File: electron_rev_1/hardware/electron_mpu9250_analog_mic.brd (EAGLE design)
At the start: 22.5 x 52.7 mm, 35 parts, among them IC4 MIC_I2S_SPH0645, U1 MPU-9250, U3 OPA322AIDBVT, U4 microSD

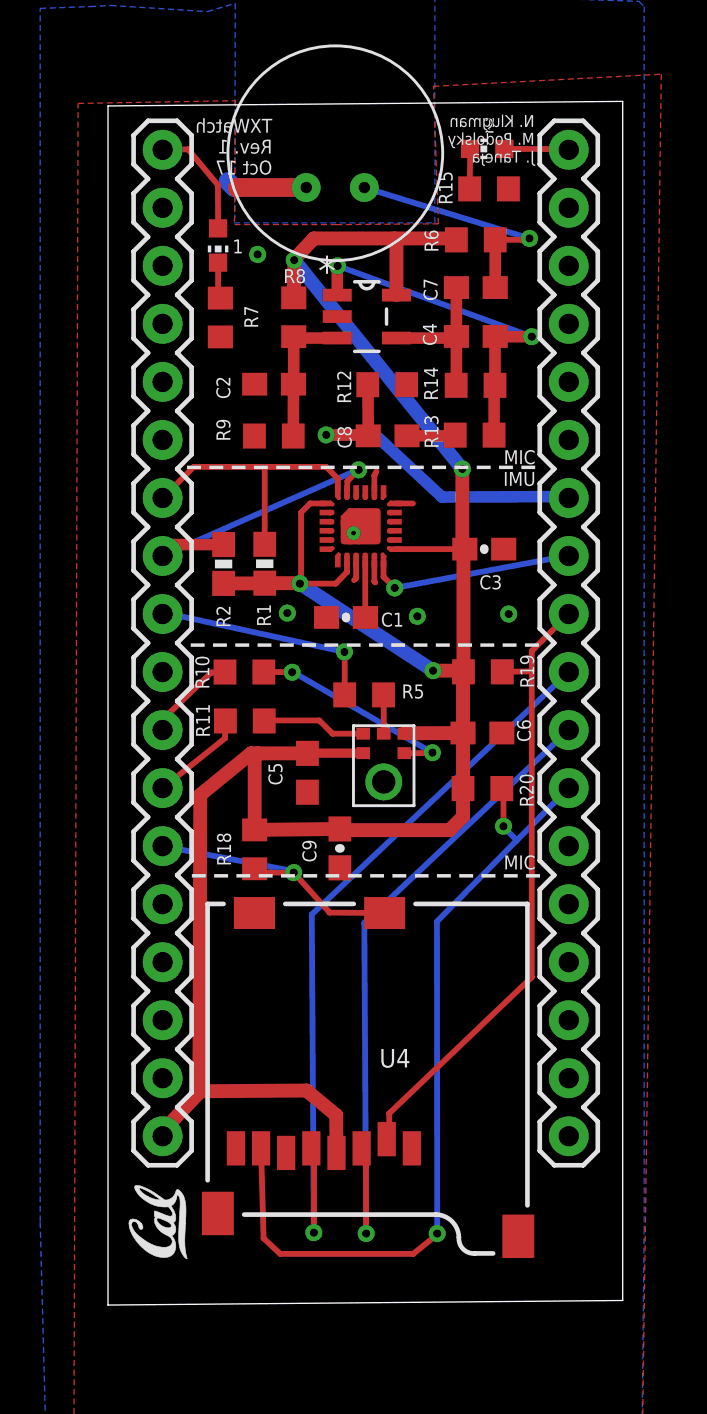
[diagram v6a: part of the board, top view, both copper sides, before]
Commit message: reroute w out gas sensor. almost ready to ship
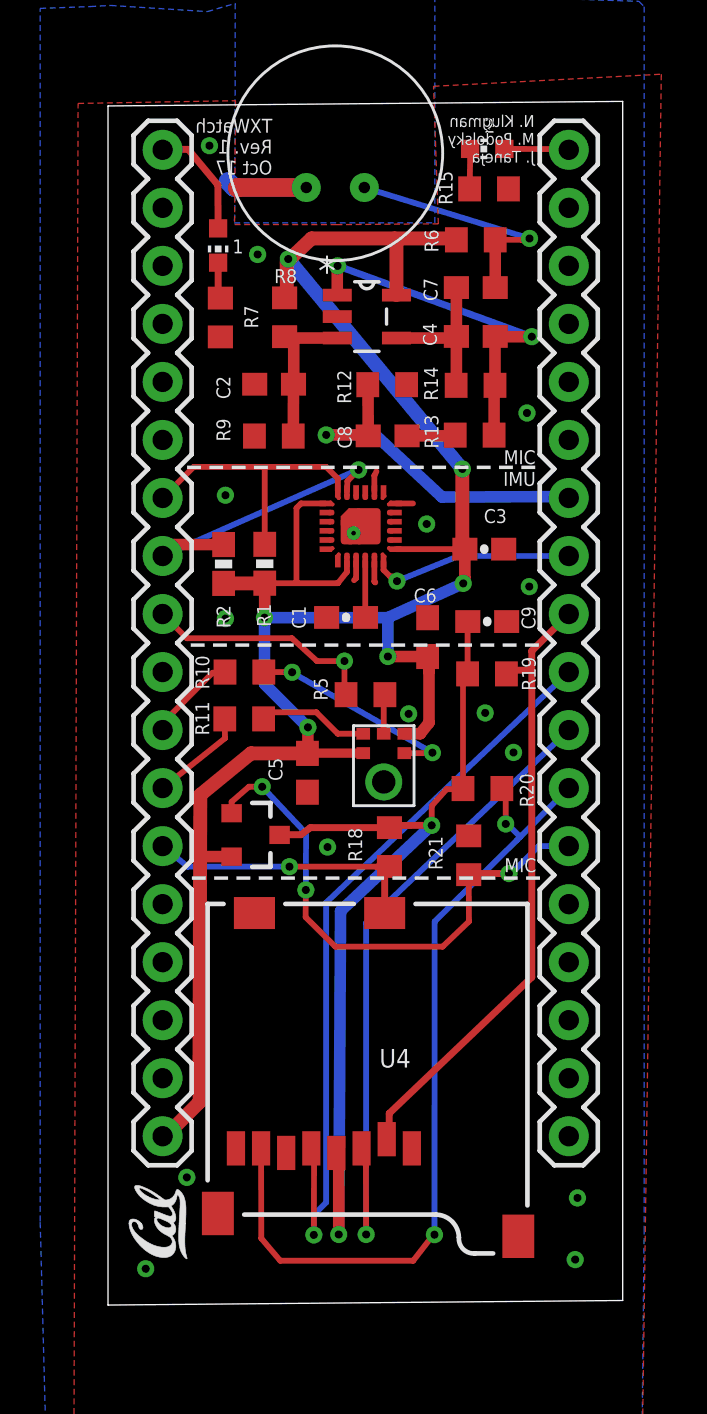
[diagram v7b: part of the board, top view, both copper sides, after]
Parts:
- added Q2: NX3008PBK, fets:SOT23-3
- added R21: 10K, resistor:R0603
- moved C9 11.8 mm to (15.8, 24.0), turned to 0 degrees
- moved R18 5.90 mm to (11.5, 14.2)
- moved C6 4.84 mm to (13.1, 23.4), turned to 90 degrees
- moved R8 0.40 mm to (6.88, 37.4)
- moved R19 0.20 mm to (15.7, 21.7)
- moved R11 0.09 mm to (5.11, 19.8)
- moved R5 0.06 mm to (10.4, 20.8)
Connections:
- new net N$10: C9.1, Q2.3, R18.2, R19.2, R20.2, U4.4
- net EN: now also Q2.1, R21.2
- net GND: now also R21.1
- net VCC: now also Q2.2; no longer C9.1, R18.2, R19.2, R20.2, U4.4
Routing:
- net N$10: track 0.00 -> 41.3 mm, vias 0 -> 2
- net EN: track 0.00 -> 23.9 mm, vias 0 -> 3
- net VCC: track 108.8 -> 93.7 mm, vias 4 -> 6
- net GND: vias 5 -> 16

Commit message: production
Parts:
- moved R18 0.17 mm to (11.3, 14.1)
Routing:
- net GND: vias 16 -> 20
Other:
- board size 22.5 x 52.7 mm -> 22.4 x 52.4 mm
